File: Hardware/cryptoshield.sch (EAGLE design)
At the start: 41 parts, among them J1 AVR_SPI_PRG_6PTH, Q1 BSS138, Q2 BSS138, U1 33mhz

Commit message: Changes 5V to IOREF
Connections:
- removed net 5V: C1.1, C10.1, R4.1, R5.1, U$1.5V, U$8.5V, U$8.RES
- new net VCCIO: C1.1, C10.1, R4.1, R5.1, U$1.IOREF, U$8.5V, U$8.RES
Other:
- note added: "Revision History: v01: Initial v02: Changed 5V to IOREF"
- note added: "v02"
- note removed: "To enable 5V logic: 1. Move solder blob to other position on 3-way jumper. 2. Place new solder blob on second jumper."
- note removed: "v01"
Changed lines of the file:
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@@
 <?xml version="1.0" encoding="utf-8"?>
 <!DOCTYPE eagle SYSTEM "eagle.dtd">
-<eagle version="6.5.0">
+<eagle version="6.4">
 <drawing>
 <settings>
@@
 <part name="R4" library="SparkFun" deviceset="RESISTOR" device="0603-RES" value="10K"/>
 <part name="SUPPLY2" library="SparkFun-Aesthetics" deviceset="3.3V" device=""/>
-<part name="SUPPLY3" library="SparkFun-Aesthetics" deviceset="5V" device=""/>
 <part name="Q2" library="SparkFun-DiscreteSemi" deviceset="MOSFET-NCHANNEL" device="BSS138" value="BSS138"/>
 <part name="R1" library="SparkFun" deviceset="RESISTOR" device="0603-RES" value="10K"/>
 <part name="R5" library="SparkFun" deviceset="RESISTOR" device="0603-RES" value="10K"/>
 <part name="SUPPLY5" library="SparkFun-Aesthetics" deviceset="3.3V" device=""/>
-<part name="SUPPLY8" library="SparkFun-Aesthetics" deviceset="5V" device=""/>
 <part name="U$8" library="SparkFun-RF" deviceset="ID-12/20" device="SMD"/>
 <part name="S1" library="SparkFun-Electromechanical" deviceset="TAC_SWITCH" device="SMD"/>
@@
 <part name="SUPPLY19" library="SparkFun-Aesthetics" deviceset="3.3V" device=""/>
 <part name="GND7" library="SparkFun-Aesthetics" deviceset="GND" device=""/>
-<part name="SUPPLY20" library="SparkFun-Aesthetics" deviceset="5V" device=""/>
 <part name="JP4" library="SparkFun-Connectors" deviceset="M06" device="NO_SILK"/>
 <part name="C1" library="SparkFun-Capacitors" deviceset="10UF50V20%(1210)" device="" value="10uF"/>
@@
 <part name="SJ1" library="SparkFun-Passives" deviceset="JUMPER-PAD-2-NO" device="YES_SILK" value=""/>
 <part name="SJ2" library="SparkFun-Passives" deviceset="JUMPER-PAD-2-NO" device="YES_SILK" value=""/>
-<part name="SUPPLY1" library="SparkFun-Aesthetics" deviceset="5V" device=""/>
-<part name="SUPPLY4" library="SparkFun-Aesthetics" deviceset="5V" device=""/>
-<part name="SUPPLY11" library="SparkFun-Aesthetics" deviceset="5V" device=""/>
-<part name="SUPPLY18" library="SparkFun-Aesthetics" deviceset="5V" device=""/>
+<part name="SUPPLY22" library="SparkFun-Aesthetics" deviceset="VCCIO" device=""/>
+<part name="SUPPLY3" library="SparkFun-Aesthetics" deviceset="VCCIO" device=""/>
+<part name="SUPPLY8" library="SparkFun-Aesthetics" deviceset="VCCIO" device=""/>
+<part name="SUPPLY1" library="SparkFun-Aesthetics" deviceset="VCCIO" device=""/>
+<part name="SUPPLY4" library="SparkFun-Aesthetics" deviceset="VCCIO" device=""/>
+<part name="SUPPLY11" library="SparkFun-Aesthetics" deviceset="VCCIO" device=""/>
+<part name="SUPPLY18" library="SparkFun-Aesthetics" deviceset="VCCIO" device=""/>
 </parts>
 <sheets>
@@
 <wire x1="142.24" y1="60.96" x2="142.24" y2="116.84" width="0.1524" layer="94"/>
 <wire x1="142.24" y1="60.96" x2="142.24" y2="0" width="0.1524" layer="94"/>
-<text x="332.74" y="116.84" size="2.54" layer="94" font="vector">I2C Level Conversion</text>
+<text x="337.82" y="132.08" size="2.54" layer="94" font="vector">I2C Level Conversion</text>
 <text x="38.1" y="5.08" size="2.54" layer="94" font="vector">Real Time Clock (w/ Battery)</text>
 <text x="226.06" y="200.66" size="2.54" layer="94" font="vector">Atmel Trusted Platform Module (TPM)</text>
@@
 <wire x1="330.2" y1="60.96" x2="431.8" y2="60.96" width="0.1524" layer="94"/>
 <wire x1="431.8" y1="60.96" x2="431.8" y2="58.42" width="0.1524" layer="94"/>
-<text x="302.26" y="93.98" size="2.54" layer="94" font="vector">To enable 5V logic:
-1. Move solder blob to other position on 3-way jumper.
-2. Place new solder blob on second jumper.</text>
 <wire x1="142.24" y1="116.84" x2="231.14" y2="116.84" width="0.1524" layer="94"/>
 <wire x1="231.14" y1="116.84" x2="231.14" y2="60.96" width="0.1524" layer="94"/>
@@
 <text x="365.76" y="36.068" size="2.54" layer="94" font="vector">AES-128 (ATAES132)</text>
 <text x="350.52" y="10.16" size="2.54" layer="94">Josh Datko / Casey Kuhns</text>
-<text x="421.64" y="7.62" size="2.54" layer="94">v01</text>
+<text x="421.64" y="7.62" size="2.54" layer="94">v02</text>
 <wire x1="0" y1="187.96" x2="142.24" y2="187.96" width="0.1524" layer="94"/>
 <text x="48.26" y="200.66" size="2.54" layer="94" font="vector">Shield Headers</text>
 <wire x1="231.14" y1="187.96" x2="231.14" y2="116.84" width="0.1524" layer="94"/>
+<wire x1="287.02" y1="116.84" x2="431.8" y2="116.84" width="0.1524" layer="94"/>
+<text x="309.88" y="78.74" size="2.54" layer="94" font="vector">Revision History:
+v01: Initial
+v02: Changed 5V to IOREF</text>
 </plain>
 <instances>
@@
 <instance part="R4" gate="G$1" x="332.74" y="154.94" rot="R270"/>
 <instance part="SUPPLY2" gate="G$1" x="317.5" y="165.1"/>
-<instance part="SUPPLY3" gate="G$1" x="332.74" y="165.1"/>
 <instance part="Q2" gate="G$1" x="388.62" y="157.48" smashed="yes" rot="R270">
 <attribute name="NAME" x="384.81" y="162.306" size="1.778" layer="95"/>
@@
 <instance part="R5" gate="G$1" x="396.24" y="165.1" rot="R270"/>
 <instance part="SUPPLY5" gate="G$1" x="381" y="175.26"/>
-<instance part="SUPPLY8" gate="G$1" x="396.24" y="175.26"/>
 <instance part="U$8" gate="G$1" x="60.96" y="154.94"/>
 <instance part="S1" gate="S" x="35.56" y="20.32"/>
@@
 <instance part="SUPPLY19" gate="G$1" x="264.16" y="172.72"/>
 <instance part="GND7" gate="1" x="274.32" y="142.24"/>
-<instance part="SUPPLY20" gate="G$1" x="38.1" y="269.24"/>
 <instance part="JP4" gate="G$1" x="246.38" y="160.02"/>
 <instance part="C1" gate="G$1" x="12.7" y="154.94"/>
@@
 <instance part="SJ1" gate="G$1" x="30.48" y="251.46"/>
 <instance part="SJ2" gate="G$1" x="22.86" y="248.92"/>
-<instance part="SUPPLY1" gate="G$1" x="35.56" y="172.72"/>
-<instance part="SUPPLY4" gate="G$1" x="78.74" y="172.72"/>
-<instance part="SUPPLY11" gate="G$1" x="12.7" y="172.72"/>
+<instance part="SUPPLY22" gate="G$1" x="38.1" y="271.78"/>
+<instance part="SUPPLY3" gate="G$1" x="332.74" y="165.1"/>
+<instance part="SUPPLY8" gate="G$1" x="396.24" y="175.26"/>
+<instance part="SUPPLY1" gate="G$1" x="12.7" y="172.72"/>
+<instance part="SUPPLY4" gate="G$1" x="35.56" y="172.72"/>
+<instance part="SUPPLY11" gate="G$1" x="78.74" y="172.72"/>
 <instance part="SUPPLY18" gate="G$1" x="109.22" y="170.18"/>
 </instances>
@@
 </segment>
 </net>
-<net name="5V" class="0">
-<segment>
-<wire x1="332.74" y1="160.02" x2="332.74" y2="165.1" width="0.1524" layer="91"/>
-<pinref part="R4" gate="G$1" pin="1"/>
-<pinref part="SUPPLY3" gate="G$1" pin="5V"/>
-</segment>
-<segment>
-<wire x1="396.24" y1="170.18" x2="396.24" y2="175.26" width="0.1524" layer="91"/>
-<pinref part="R5" gate="G$1" pin="1"/>
-<pinref part="SUPPLY8" gate="G$1" pin="5V"/>
-</segment>
-<segment>
-<pinref part="U$1" gate="G$1" pin="5V"/>
-<pinref part="SUPPLY20" gate="G$1" pin="5V"/>
-<wire x1="50.8" y1="233.68" x2="38.1" y2="233.68" width="0.1524" layer="91"/>
-<wire x1="38.1" y1="233.68" x2="38.1" y2="269.24" width="0.1524" layer="91"/>
-</segment>
-<segment>
-<pinref part="U$8" gate="G$1" pin="RES"/>
-<wire x1="45.72" y1="154.94" x2="35.56" y2="154.94" width="0.1524" layer="91"/>
-<wire x1="35.56" y1="154.94" x2="35.56" y2="172.72" width="0.1524" layer="91"/>
-<pinref part="SUPPLY1" gate="G$1" pin="5V"/>
-</segment>
-<segment>
-<wire x1="78.74" y1="172.72" x2="78.74" y2="162.56" width="0.1524" layer="91"/>
-<pinref part="U$8" gate="G$1" pin="5V"/>
-<wire x1="76.2" y1="162.56" x2="78.74" y2="162.56" width="0.1524" layer="91"/>
-<pinref part="SUPPLY4" gate="G$1" pin="5V"/>
-</segment>
-<segment>
-<pinref part="C1" gate="G$1" pin="1"/>
-<wire x1="12.7" y1="160.02" x2="12.7" y2="172.72" width="0.1524" layer="91"/>
-<pinref part="SUPPLY11" gate="G$1" pin="5V"/>
-</segment>
-<segment>
-<pinref part="C10" gate="G$1" pin="1"/>
-<wire x1="109.22" y1="157.48" x2="109.22" y2="170.18" width="0.1524" layer="91"/>
-<pinref part="SUPPLY18" gate="G$1" pin="5V"/>
-</segment>
-</net>
 <net name="SDA_IN" class="0">
 <segment>
@@
 </segment>
 </net>
+<net name="VCCIO" class="0">
+<segment>
+<pinref part="U$1" gate="G$1" pin="IOREF"/>
+<wire x1="50.8" y1="241.3" x2="38.1" y2="241.3" width="0.1524" layer="91"/>
+<wire x1="38.1" y1="241.3" x2="38.1" y2="271.78" width="0.1524" layer="91"/>
+<pinref part="SUPPLY22" gate="G$1" pin="VCCIO"/>
+</segment>
+<segment>
+<wire x1="332.74" y1="160.02" x2="332.74" y2="165.1" width="0.1524" layer="91"/>
+<pinref part="R4" gate="G$1" pin="1"/>
+<pinref part="SUPPLY3" gate="G$1" pin="VCCIO"/>
+</segment>
+<segment>
+<wire x1="396.24" y1="170.18" x2="396.24" y2="175.26" width="0.1524" layer="91"/>
+<pinref part="R5" gate="G$1" pin="1"/>
+<pinref part="SUPPLY8" gate="G$1" pin="VCCIO"/>
+</segment>
+<segment>
+<pinref part="U$8" gate="G$1" pin="RES"/>
+<wire x1="45.72" y1="154.94" x2="35.56" y2="154.94" width="0.1524" layer="91"/>
+<wire x1="35.56" y1="154.94" x2="35.56" y2="172.72" width="0.1524" layer="91"/>
+<pinref part="SUPPLY4" gate="G$1" pin="VCCIO"/>
+</segment>
+<segment>
+<wire x1="78.74" y1="172.72" x2="78.74" y2="162.56" width="0.1524" layer="91"/>
+<pinref part="U$8" gate="G$1" pin="5V"/>
+<wire x1="76.2" y1="162.56" x2="78.74" y2="162.56" width="0.1524" layer="91"/>
+<pinref part="SUPPLY11" gate="G$1" pin="VCCIO"/>
+</segment>
+<segment>
+<pinref part="C1" gate="G$1" pin="1"/>
+<wire x1="12.7" y1="160.02" x2="12.7" y2="172.72" width="0.1524" layer="91"/>
+<pinref part="SUPPLY1" gate="G$1" pin="VCCIO"/>
+</segment>
+<segment>
+<pinref part="C10" gate="G$1" pin="1"/>
+<wire x1="109.22" y1="157.48" x2="109.22" y2="170.18" width="0.1524" layer="91"/>
+<pinref part="SUPPLY18" gate="G$1" pin="VCCIO"/>
+</segment>
+</net>

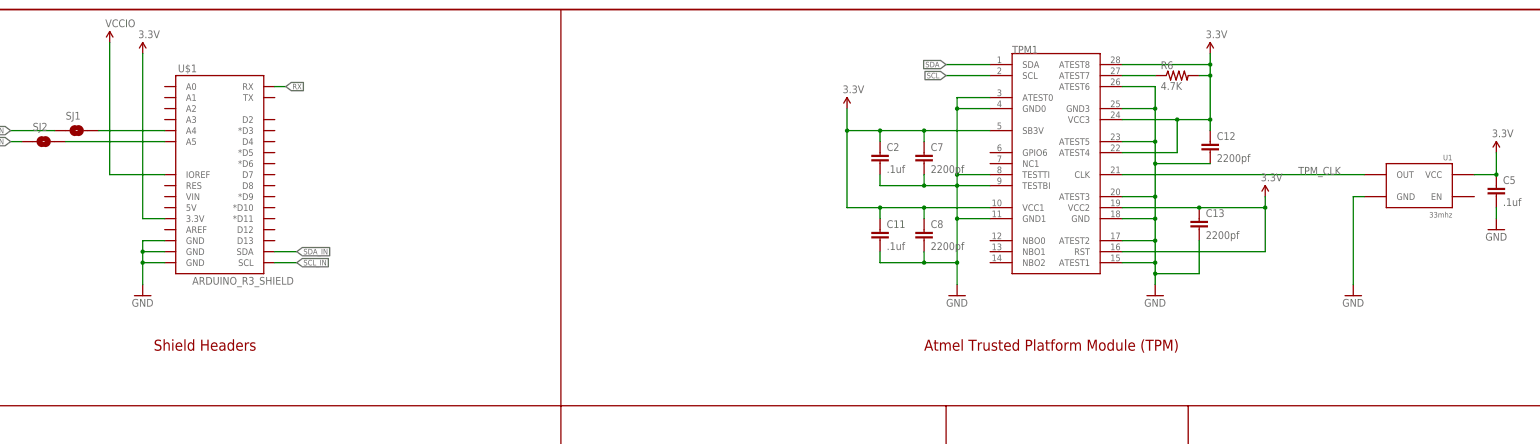
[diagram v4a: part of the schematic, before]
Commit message: added mosfet reset circuit to couple TPM reset to Arduino Reset pin
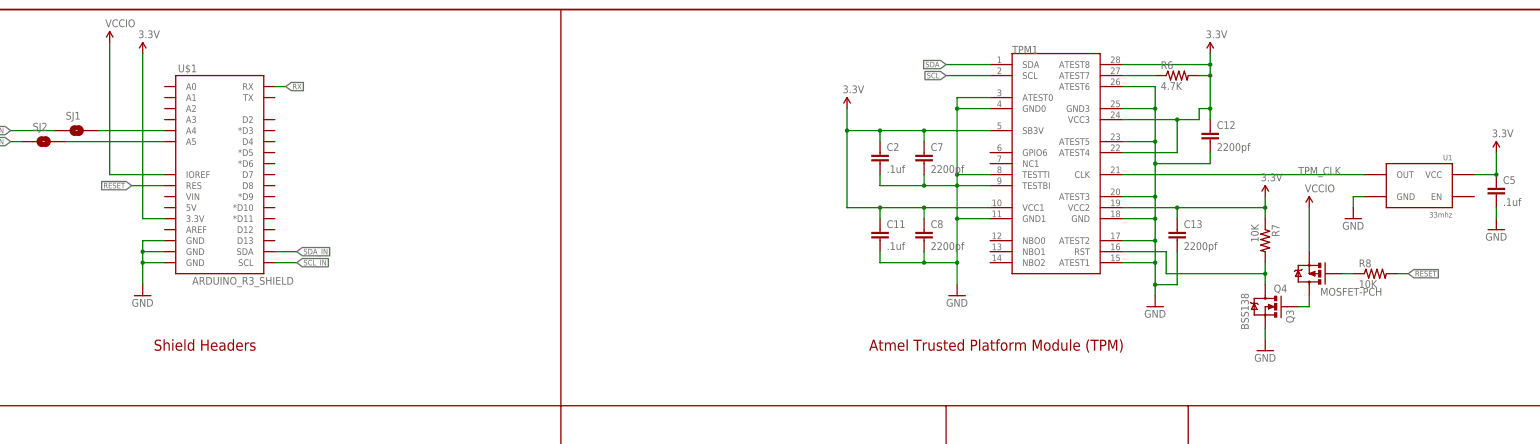
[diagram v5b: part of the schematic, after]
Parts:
- added Q3: BSS138, SparkFun-DiscreteSemi:MOSFET-NCHANNELBSS138
- added Q4: MOSFET-PCH, SparkFun-DiscreteSemi:MOSFET-PCHANNEL
- added R7, R8: 10K, SparkFun:RESISTOR0603-RES
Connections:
- new net !RESET: R8.2, U$1.RES
- new net N$18: Q3.D, R7.2, TPM1.RST
- new net N$20: Q3.G, Q4.D
- new net N$21: Q4.G, R8.1
- net 3.3V: now also R7.1; no longer TPM1.RST
- net GND: now also Q3.S
- net VCCIO: now also Q4.S
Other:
- moved on the sheet: C12, C13
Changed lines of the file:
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@@
 <?xml version="1.0" encoding="utf-8"?>
 <!DOCTYPE eagle SYSTEM "eagle.dtd">
-<eagle version="6.4">
+<eagle version="6.5.0">
 <drawing>
 <settings>
@@
 <part name="SUPPLY11" library="SparkFun-Aesthetics" deviceset="VCCIO" device=""/>
 <part name="SUPPLY18" library="SparkFun-Aesthetics" deviceset="VCCIO" device=""/>
+<part name="Q3" library="SparkFun-DiscreteSemi" deviceset="MOSFET-NCHANNEL" device="BSS138" value="BSS138"/>
+<part name="R7" library="SparkFun" deviceset="RESISTOR" device="0603-RES" value="10K"/>
+<part name="GND10" library="supply1" deviceset="GND" device=""/>
+<part name="Q4" library="SparkFun-DiscreteSemi" deviceset="MOSFET-PCHANNEL" device="" value="MOSFET-PCH"/>
+<part name="SUPPLY20" library="SparkFun-Aesthetics" deviceset="VCCIO" device=""/>
+<part name="R8" library="SparkFun" deviceset="RESISTOR" device="0603-RES" value="10K"/>
 </parts>
 <sheets>
@@
 <text x="337.82" y="132.08" size="2.54" layer="94" font="vector">I2C Level Conversion</text>
 <text x="38.1" y="5.08" size="2.54" layer="94" font="vector">Real Time Clock (w/ Battery)</text>
-<text x="226.06" y="200.66" size="2.54" layer="94" font="vector">Atmel Trusted Platform Module (TPM)</text>
+<text x="213.36" y="200.66" size="2.54" layer="94" font="vector">Atmel Trusted Platform Module (TPM)</text>
 <wire x1="142.24" y1="187.96" x2="231.14" y2="187.96" width="0.1524" layer="94"/>
 <wire x1="231.14" y1="187.96" x2="287.02" y2="187.96" width="0.1524" layer="94"/>
@@
 <instance part="GND5" gate="1" x="149.86" y="15.24"/>
 <instance part="GND3" gate="1" x="233.68" y="213.36"/>
-<instance part="GND4" gate="1" x="279.4" y="213.36"/>
+<instance part="GND4" gate="1" x="279.4" y="210.82"/>
 <instance part="C2" gate="G$1" x="215.9" y="243.84"/>
 <instance part="C7" gate="G$1" x="226.06" y="243.84"/>
 <instance part="C8" gate="G$1" x="226.06" y="226.06"/>
 <instance part="C11" gate="G$1" x="215.9" y="226.06"/>
-<instance part="C12" gate="G$1" x="292.1" y="246.38"/>
-<instance part="C13" gate="G$1" x="289.56" y="228.6"/>
+<instance part="C12" gate="G$1" x="292.1" y="248.92"/>
+<instance part="C13" gate="G$1" x="284.48" y="226.06"/>
 <instance part="FRAME1" gate="G$1" x="0" y="0"/>
 <instance part="FRAME1" gate="G$2" x="330.2" y="0"/>
@@
 <instance part="U1" gate="G$1" x="340.36" y="238.76" rot="MR0"/>
 <instance part="SUPPLY17" gate="G$1" x="358.14" y="246.38"/>
-<instance part="GND18" gate="1" x="325.12" y="213.36"/>
+<instance part="GND18" gate="1" x="325.12" y="231.14"/>
 <instance part="C5" gate="G$1" x="358.14" y="236.22"/>
 <instance part="GND19" gate="1" x="358.14" y="228.6"/>
@@
 <instance part="SUPPLY11" gate="G$1" x="78.74" y="172.72"/>
 <instance part="SUPPLY18" gate="G$1" x="109.22" y="170.18"/>
+<instance part="Q3" gate="G$1" x="304.8" y="210.82" smashed="yes" rot="MR0">
+<attribute name="NAME" x="309.626" y="207.01" size="1.778" layer="95" rot="MR90"/>
+<attribute name="VALUE" x="299.212" y="205.486" size="1.778" layer="96" rot="MR90"/>
+</instance>
+<instance part="R7" gate="G$1" x="304.8" y="226.06" rot="R270"/>
+<instance part="GND10" gate="1" x="304.8" y="200.66"/>
+<instance part="Q4" gate="G$1" x="314.96" y="218.44" smashed="yes" rot="R180">
+<attribute name="NAME" x="309.88" y="215.9" size="1.778" layer="95" rot="R180"/>
+<attribute name="VALUE" x="317.5" y="213.36" size="1.778" layer="96"/>
+</instance>
+<instance part="SUPPLY20" gate="G$1" x="314.96" y="233.68"/>
+<instance part="R8" gate="G$1" x="330.2" y="218.44"/>
 </instances>
 <busses>
@@
 <wire x1="279.4" y1="231.14" x2="279.4" y2="226.06" width="0.1524" layer="91"/>
 <wire x1="279.4" y1="226.06" x2="279.4" y2="220.98" width="0.1524" layer="91"/>
-<wire x1="279.4" y1="220.98" x2="279.4" y2="218.44" width="0.1524" layer="91"/>
-<wire x1="279.4" y1="218.44" x2="279.4" y2="215.9" width="0.1524" layer="91"/>
+<wire x1="279.4" y1="220.98" x2="279.4" y2="215.9" width="0.1524" layer="91"/>
+<wire x1="279.4" y1="215.9" x2="279.4" y2="213.36" width="0.1524" layer="91"/>
 <pinref part="C12" gate="G$1" pin="2"/>
+<wire x1="292.1" y1="246.38" x2="292.1" y2="243.84" width="0.1524" layer="91"/>
 <wire x1="292.1" y1="243.84" x2="279.4" y2="243.84" width="0.1524" layer="91"/>
 <junction x="279.4" y="243.84"/>
 <pinref part="C13" gate="G$1" pin="2"/>
-<wire x1="289.56" y1="226.06" x2="289.56" y2="218.44" width="0.1524" layer="91"/>
-<wire x1="289.56" y1="218.44" x2="279.4" y2="218.44" width="0.1524" layer="91"/>
-<junction x="279.4" y="218.44"/>
+<wire x1="284.48" y1="223.52" x2="284.48" y2="215.9" width="0.1524" layer="91"/>
+<wire x1="284.48" y1="215.9" x2="279.4" y2="215.9" width="0.1524" layer="91"/>
+<junction x="279.4" y="215.9"/>
 <pinref part="TPM1" gate="G$1" pin="ATEST6"/>
 <wire x1="271.78" y1="261.62" x2="279.4" y2="261.62" width="0.1524" layer="91"/>
@@
 <pinref part="U1" gate="G$1" pin="GND"/>
 <wire x1="327.66" y1="236.22" x2="325.12" y2="236.22" width="0.1524" layer="91"/>
-<wire x1="325.12" y1="236.22" x2="325.12" y2="215.9" width="0.1524" layer="91"/>
+<wire x1="325.12" y1="236.22" x2="325.12" y2="233.68" width="0.1524" layer="91"/>
 <pinref part="GND18" gate="1" pin="GND"/>
 </segment>
@@
 <pinref part="GND9" gate="1" pin="GND"/>
 <wire x1="109.22" y1="149.86" x2="109.22" y2="142.24" width="0.1524" layer="91"/>
+</segment>
+<segment>
+<pinref part="Q3" gate="G$1" pin="S"/>
+<pinref part="GND10" gate="1" pin="GND"/>
+<wire x1="304.8" y1="203.2" x2="304.8" y2="205.74" width="0.1524" layer="91"/>
 </segment>
 </net>
@@
 <wire x1="292.1" y1="269.24" x2="292.1" y2="266.7" width="0.1524" layer="91"/>
 <wire x1="292.1" y1="266.7" x2="292.1" y2="264.16" width="0.1524" layer="91"/>
-<wire x1="292.1" y1="264.16" x2="292.1" y2="254" width="0.1524" layer="91"/>
-<wire x1="292.1" y1="254" x2="292.1" y2="251.46" width="0.1524" layer="91"/>
+<wire x1="292.1" y1="264.16" x2="292.1" y2="256.54" width="0.1524" layer="91"/>
+<wire x1="292.1" y1="256.54" x2="292.1" y2="254" width="0.1524" layer="91"/>
 <wire x1="271.78" y1="254" x2="284.48" y2="254" width="0.1524" layer="91"/>
-<junction x="292.1" y="254"/>
+<junction x="292.1" y="256.54"/>
 <pinref part="TPM1" gate="G$1" pin="VCC3"/>
 <pinref part="TPM1" gate="G$1" pin="ATEST8"/>
-<wire x1="284.48" y1="254" x2="292.1" y2="254" width="0.1524" layer="91"/>
+<wire x1="284.48" y1="254" x2="289.56" y2="254" width="0.1524" layer="91"/>
+<wire x1="289.56" y1="254" x2="289.56" y2="256.54" width="0.1524" layer="91"/>
+<wire x1="289.56" y1="256.54" x2="292.1" y2="256.54" width="0.1524" layer="91"/>
 <wire x1="271.78" y1="266.7" x2="292.1" y2="266.7" width="0.1524" layer="91"/>
 <junction x="292.1" y="266.7"/>
@@
 <wire x1="304.8" y1="236.22" x2="304.8" y2="233.68" width="0.1524" layer="91"/>
 <pinref part="C13" gate="G$1" pin="1"/>
-<wire x1="289.56" y1="233.68" x2="271.78" y2="233.68" width="0.1524" layer="91"/>
-<wire x1="304.8" y1="233.68" x2="289.56" y2="233.68" width="0.1524" layer="91"/>
-<junction x="289.56" y="233.68"/>
+<wire x1="284.48" y1="233.68" x2="271.78" y2="233.68" width="0.1524" layer="91"/>
+<wire x1="304.8" y1="233.68" x2="284.48" y2="233.68" width="0.1524" layer="91"/>
+<wire x1="284.48" y1="233.68" x2="284.48" y2="231.14" width="0.1524" layer="91"/>
 <pinref part="TPM1" gate="G$1" pin="VCC2"/>
 <pinref part="SUPPLY10" gate="G$1" pin="3.3V"/>
-<pinref part="TPM1" gate="G$1" pin="RST"/>
-<wire x1="271.78" y1="223.52" x2="304.8" y2="223.52" width="0.1524" layer="91"/>
-<wire x1="304.8" y1="223.52" x2="304.8" y2="233.68" width="0.1524" layer="91"/>
 <junction x="304.8" y="233.68"/>
+<junction x="284.48" y="233.68"/>
+<pinref part="R7" gate="G$1" pin="1"/>
+<wire x1="304.8" y1="231.14" x2="304.8" y2="233.68" width="0.1524" layer="91"/>
 </segment>
 <segment>
@@
 <pinref part="SUPPLY18" gate="G$1" pin="VCCIO"/>
 </segment>
-</net>
+<segment>
+<pinref part="Q4" gate="G$1" pin="S"/>
+<pinref part="SUPPLY20" gate="G$1" pin="VCCIO"/>
+<wire x1="314.96" y1="233.68" x2="314.96" y2="223.52" width="0.1524" layer="91"/>
+</segment>
+</net>
+<net name="N$18" class="0">
+<segment>
+<pinref part="R7" gate="G$1" pin="2"/>
+<wire x1="304.8" y1="218.44" x2="304.8" y2="220.98" width="0.1524" layer="91"/>
+<wire x1="281.94" y1="218.44" x2="304.8" y2="218.44" width="0.1524" layer="91"/>
+<pinref part="TPM1" gate="G$1" pin="RST"/>
+<wire x1="271.78" y1="223.52" x2="281.94" y2="223.52" width="0.1524" layer="91"/>
+<wire x1="281.94" y1="223.52" x2="281.94" y2="218.44" width="0.1524" layer="91"/>
+<pinref part="Q3" gate="G$1" pin="D"/>
+<wire x1="304.8" y1="218.44" x2="304.8" y2="215.9" width="0.1524" layer="91"/>
+<junction x="304.8" y="218.44"/>
+</segment>
+</net>
+<net name="N$20" class="0">
+<segment>
+<pinref part="Q3" gate="G$1" pin="G"/>
+<pinref part="Q4" gate="G$1" pin="D"/>
+<wire x1="312.42" y1="210.82" x2="314.96" y2="210.82" width="0.1524" layer="91"/>
+<wire x1="314.96" y1="210.82" x2="314.96" y2="213.36" width="0.1524" layer="91"/>
+</segment>
+</net>
+<net name="N$21" class="0">
+<segment>
+<pinref part="Q4" gate="G$1" pin="G"/>
+<pinref part="R8" gate="G$1" pin="1"/>
+<wire x1="325.12" y1="218.44" x2="322.58" y2="218.44" width="0.1524" layer="91"/>
+</segment>
+</net>
+<net name="!RESET" class="0">
+<segment>
+<pinref part="R8" gate="G$1" pin="2"/>
+<wire x1="335.28" y1="218.44" x2="337.82" y2="218.44" width="0.1524" layer="91"/>
+<label x="337.82" y="218.44" size="1.27" layer="95" xref="yes"/>
+</segment>
+<segment>
+<pinref part="U$1" gate="G$1" pin="RES"/>
+<wire x1="50.8" y1="238.76" x2="43.18" y2="238.76" width="0.1524" layer="91"/>
+<label x="43.18" y="238.76" size="1.27" layer="95" rot="R180" xref="yes"/>
+</segment>
+</net>
